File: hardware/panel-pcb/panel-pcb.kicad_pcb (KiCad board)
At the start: 4 copper layers, 127 x 127 mm, 0 parts

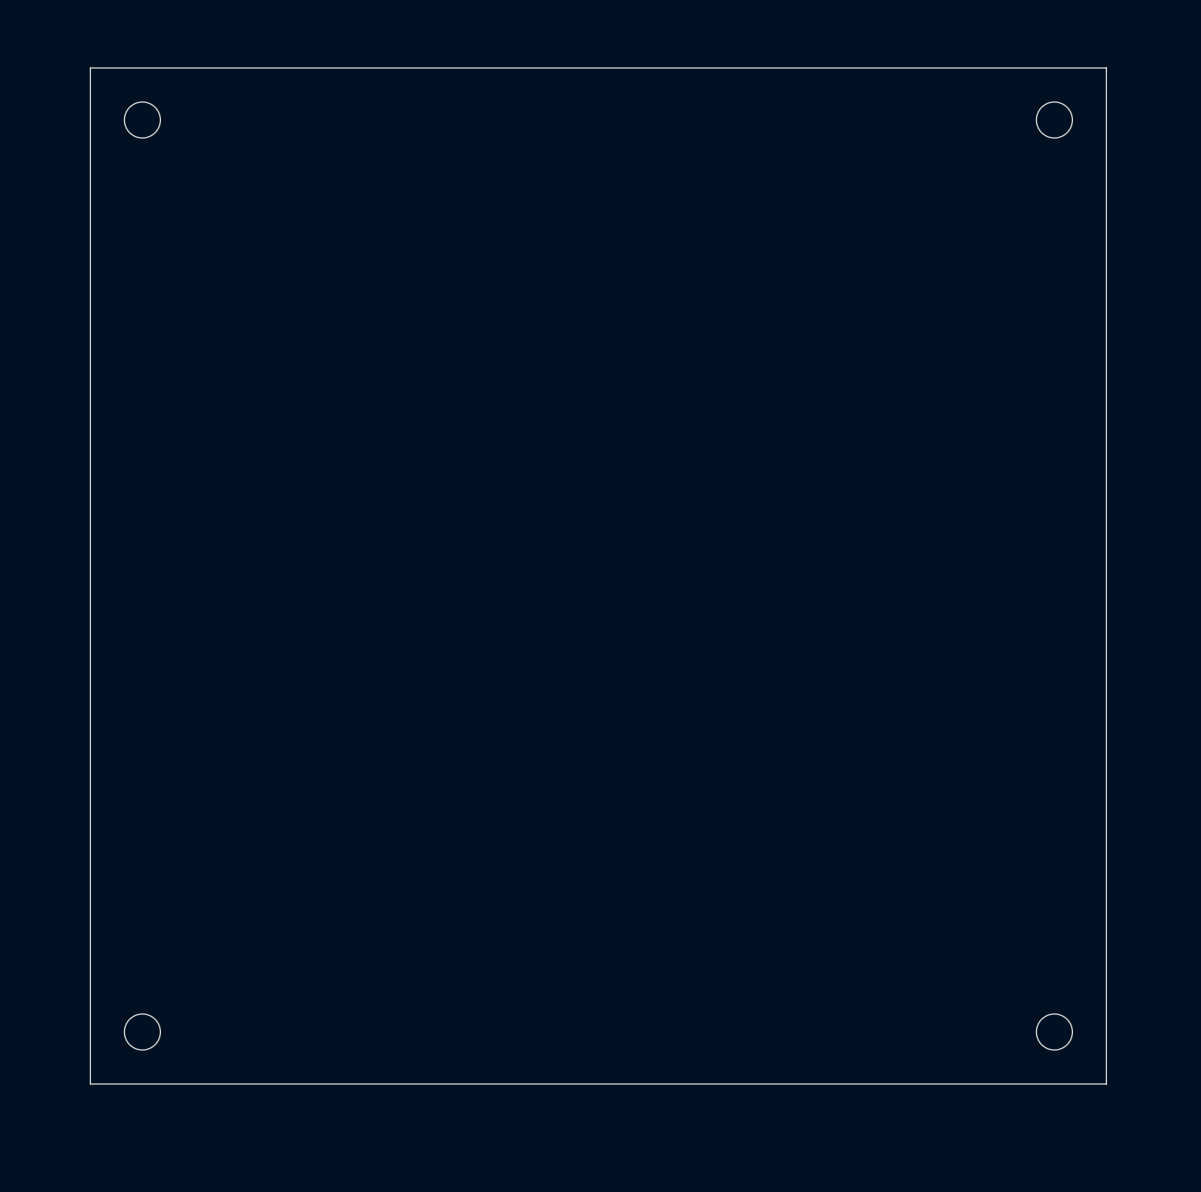
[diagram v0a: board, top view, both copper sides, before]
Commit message: PCB placement pass 1: LED lattice + all clusters
- 25x WS2815 on measured lattice (4-3-4-3-4-3-4, row 1 Y=11mm, 17mm rows,
  34mm columns, serpentine chain order derived from netlist), per-LED caps
  mid-gap below each LED
- Edge connectors at stock-measured positions (power ~25mm, INT ~93mm,
  RS-485 IN ~103mm left / OUT ~95mm right), FSR JST-PH near-centered per edge
- MCU cluster in the x148-162 lattice channel (QFN + decoupler columns,
  crystal, flash, FSR analog strip at pins), LDO cluster top-left by power IN,
  RS-485 xcvr + termination bottom-left by data connectors, shifter at LED 0,
  USB-C/SWD/BOOTSEL/ID-DIP bottom strip, TPs near their signals
- DRC: 0 shorts; remaining violations are silk/courtyard refinements
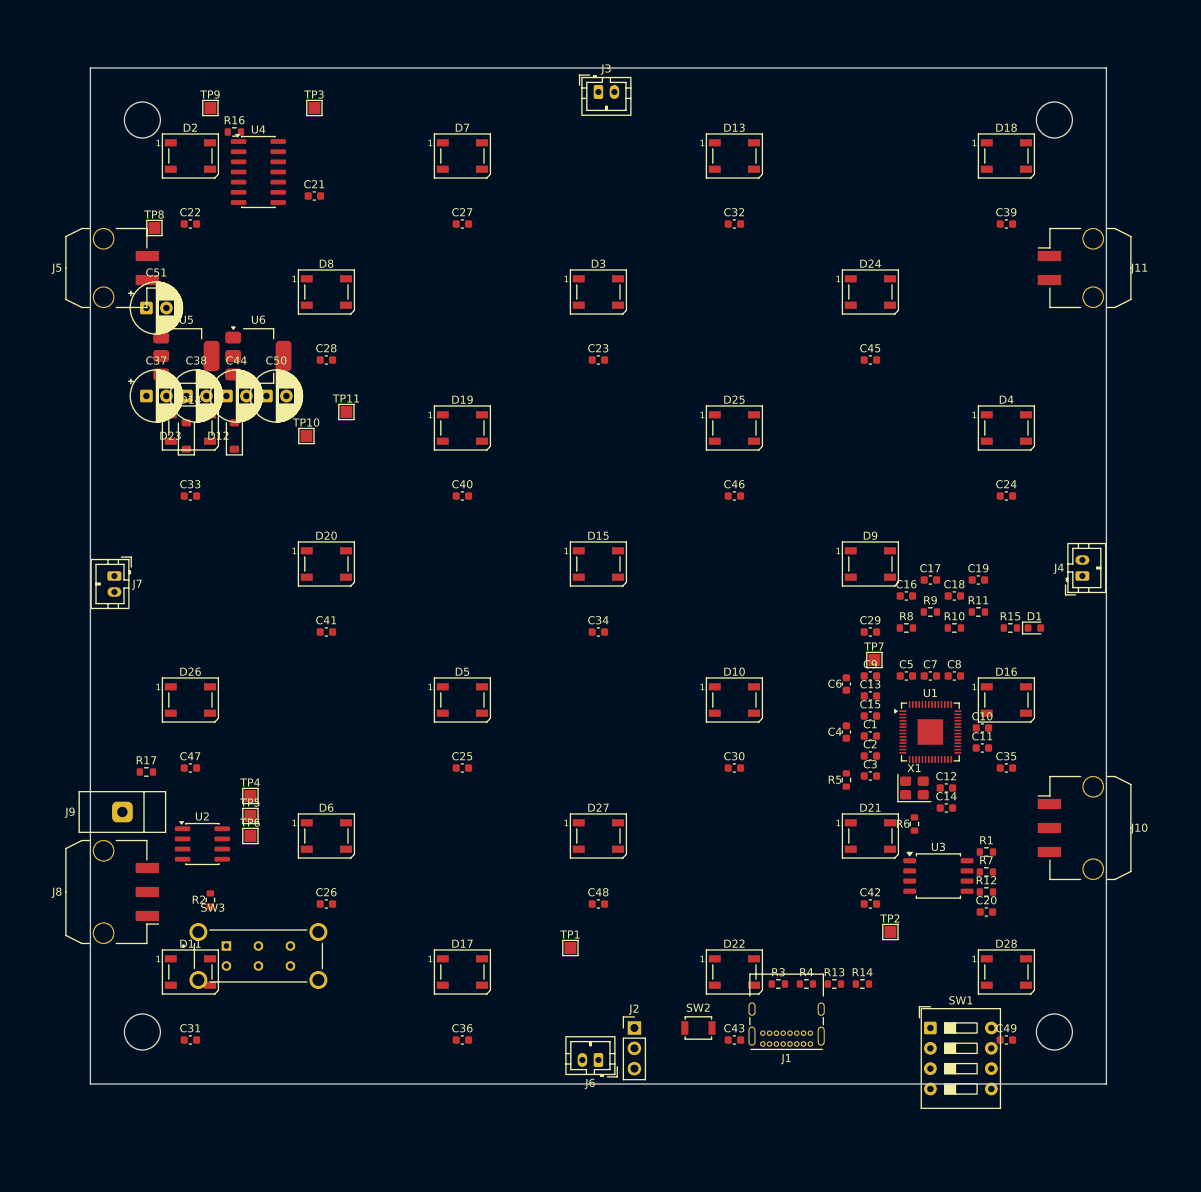
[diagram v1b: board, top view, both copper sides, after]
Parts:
- added C1: 100nF X7R 50V, Capacitor_SMD:C_0603_1608Metric, F.Cu at (147.5, 133.5)
- added C10: 100nF X7R 50V, Capacitor_SMD:C_0603_1608Metric, F.Cu at (161.5, 132.5)
- added C11: 100nF X7R 50V, Capacitor_SMD:C_0603_1608Metric, F.Cu at (161.5, 135.0)
- added C12: 15pF C0G 50V, Capacitor_SMD:C_0603_1608Metric, F.Cu at (157.0, 140.0)
- added C13: 100nF X7R 50V, Capacitor_SMD:C_0603_1608Metric, F.Cu at (147.5, 128.5)
- added C14: 15pF C0G 50V, Capacitor_SMD:C_0603_1608Metric, F.Cu at (157.0, 142.5)
- added C15: 100nF X7R 50V, Capacitor_SMD:C_0603_1608Metric, F.Cu at (147.5, 131.0)
- added C16: 10nF C0G 50V, Capacitor_SMD:C_0603_1608Metric, F.Cu at (152.0, 116.0)
- added C17: 10nF C0G 50V, Capacitor_SMD:C_0603_1608Metric, F.Cu at (155.0, 114.0)
- added C18: 10nF C0G 50V, Capacitor_SMD:C_0603_1608Metric, F.Cu at (158.0, 116.0)
- added C19: 10nF C0G 50V, Capacitor_SMD:C_0603_1608Metric, F.Cu at (161.0, 114.0)
- added C2: 100nF X7R 50V, Capacitor_SMD:C_0603_1608Metric, F.Cu at (147.5, 136.0)
- added C20: 100nF X7R 50V, Capacitor_SMD:C_0603_1608Metric, F.Cu at (162.0, 155.5)
- added C21: 100nF X7R 50V, Capacitor_SMD:C_0603_1608Metric, F.Cu at (78.0, 66.0)
- added C22: 100nF X7R 50V, Capacitor_SMD:C_0603_1608Metric, F.Cu at (62.5, 69.5)
- added C23: 100nF X7R 50V, Capacitor_SMD:C_0603_1608Metric, F.Cu at (113.5, 86.5)
- added C24: 100nF X7R 50V, Capacitor_SMD:C_0603_1608Metric, F.Cu at (164.5, 103.5)
- added C25: 100nF X7R 50V, Capacitor_SMD:C_0603_1608Metric, F.Cu at (96.5, 137.5)
- added C26: 100nF X7R 50V, Capacitor_SMD:C_0603_1608Metric, F.Cu at (79.5, 154.5)
- added C27: 100nF X7R 50V, Capacitor_SMD:C_0603_1608Metric, F.Cu at (96.5, 69.5)
- added C28: 100nF X7R 50V, Capacitor_SMD:C_0603_1608Metric, F.Cu at (79.5, 86.5)
- added C29: 100nF X7R 50V, Capacitor_SMD:C_0603_1608Metric, F.Cu at (147.5, 120.5)
- added C3: 100nF X7R 50V, Capacitor_SMD:C_0603_1608Metric, F.Cu at (147.5, 138.5)
- added C30: 100nF X7R 50V, Capacitor_SMD:C_0603_1608Metric, F.Cu at (130.5, 137.5)
- added C31: 100nF X7R 50V, Capacitor_SMD:C_0603_1608Metric, F.Cu at (62.5, 171.5)
- added C32: 100nF X7R 50V, Capacitor_SMD:C_0603_1608Metric, F.Cu at (130.5, 69.5)
- added C33: 100nF X7R 50V, Capacitor_SMD:C_0603_1608Metric, F.Cu at (62.5, 103.5)
- added C34: 100nF X7R 50V, Capacitor_SMD:C_0603_1608Metric, F.Cu at (113.5, 120.5)
- added C35: 100nF X7R 50V, Capacitor_SMD:C_0603_1608Metric, F.Cu at (164.5, 137.5)
- added C36: 100nF X7R 50V, Capacitor_SMD:C_0603_1608Metric, F.Cu at (96.5, 171.5)
- added C37: 10uF elec 25V, Capacitor_THT:CP_Radial_D6.3mm_P2.50mm, F.Cu at (57.0, 91.0)
- added C38: 22uF elec 25V, Capacitor_THT:CP_Radial_D6.3mm_P2.50mm, F.Cu at (62.0, 91.0)
- added C39: 100nF X7R 50V, Capacitor_SMD:C_0603_1608Metric, F.Cu at (164.5, 69.5)
- added C4: 2.2uF X5R 16V, Capacitor_SMD:C_0603_1608Metric, F.Cu at (144.5, 133.0)
- added C40: 100nF X7R 50V, Capacitor_SMD:C_0603_1608Metric, F.Cu at (96.5, 103.5)
- added C41: 100nF X7R 50V, Capacitor_SMD:C_0603_1608Metric, F.Cu at (79.5, 120.5)
- added C42: 100nF X7R 50V, Capacitor_SMD:C_0603_1608Metric, F.Cu at (147.5, 154.5)
- added C43: 100nF X7R 50V, Capacitor_SMD:C_0603_1608Metric, F.Cu at (130.5, 171.5)
- added C44: 10uF elec 25V, Capacitor_THT:CP_Radial_D6.3mm_P2.50mm, F.Cu at (67.0, 91.0)
- added C45: 100nF X7R 50V, Capacitor_SMD:C_0603_1608Metric, F.Cu at (147.5, 86.5)
- added C46: 100nF X7R 50V, Capacitor_SMD:C_0603_1608Metric, F.Cu at (130.5, 103.5)
- added C47: 100nF X7R 50V, Capacitor_SMD:C_0603_1608Metric, F.Cu at (62.5, 137.5)
- added C48: 100nF X7R 50V, Capacitor_SMD:C_0603_1608Metric, F.Cu at (113.5, 154.5)
- added C49: 100nF X7R 50V, Capacitor_SMD:C_0603_1608Metric, F.Cu at (164.5, 171.5)
- added C5: 100nF X7R 50V, Capacitor_SMD:C_0603_1608Metric, F.Cu at (152.0, 126.0)
- added C50: 22uF elec 25V, Capacitor_THT:CP_Radial_D6.3mm_P2.50mm, F.Cu at (72.0, 91.0)
- added C51: 470uF elec 25V, Capacitor_THT:CP_Radial_D6.3mm_P2.50mm, F.Cu at (57.0, 80.0)
- added C6: 1uF X5R 16V, Capacitor_SMD:C_0603_1608Metric, F.Cu at (144.5, 127.0)
- added C7: 100nF X7R 50V, Capacitor_SMD:C_0603_1608Metric, F.Cu at (155.0, 126.0)
- added C8: 100nF X7R 50V, Capacitor_SMD:C_0603_1608Metric, F.Cu at (158.0, 126.0)
- added C9: 1uF X5R 16V, Capacitor_SMD:C_0603_1608Metric, F.Cu at (147.5, 126.0)
- added D1: DEBUG, LED_SMD:LED_0603_1608Metric, F.Cu at (168.0, 120.0)
- added D10: WS2815, LED_SMD:LED_WS2812B_PLCC4_5.0x5.0mm_P3.2mm, F.Cu at (130.5, 129.0)
- added D11: WS2815, LED_SMD:LED_WS2812B_PLCC4_5.0x5.0mm_P3.2mm, F.Cu at (62.5, 163.0)
- added D12: 1N5819W, Diode_SMD:D_SOD-123, F.Cu at (68.0, 96.0)
- added D13: WS2815, LED_SMD:LED_WS2812B_PLCC4_5.0x5.0mm_P3.2mm, F.Cu at (130.5, 61.0)
- added D14: WS2815, LED_SMD:LED_WS2812B_PLCC4_5.0x5.0mm_P3.2mm, F.Cu at (62.5, 95.0)
- added D15: WS2815, LED_SMD:LED_WS2812B_PLCC4_5.0x5.0mm_P3.2mm, F.Cu at (113.5, 112.0)
- added D16: WS2815, LED_SMD:LED_WS2812B_PLCC4_5.0x5.0mm_P3.2mm, F.Cu at (164.5, 129.0)
- added D17: WS2815, LED_SMD:LED_WS2812B_PLCC4_5.0x5.0mm_P3.2mm, F.Cu at (96.5, 163.0)
- added D18: WS2815, LED_SMD:LED_WS2812B_PLCC4_5.0x5.0mm_P3.2mm, F.Cu at (164.5, 61.0)
- added D19: WS2815, LED_SMD:LED_WS2812B_PLCC4_5.0x5.0mm_P3.2mm, F.Cu at (96.5, 95.0)
- added D2: WS2815, LED_SMD:LED_WS2812B_PLCC4_5.0x5.0mm_P3.2mm, F.Cu at (62.5, 61.0)
- added D20: WS2815, LED_SMD:LED_WS2812B_PLCC4_5.0x5.0mm_P3.2mm, F.Cu at (79.5, 112.0)
- added D21: WS2815, LED_SMD:LED_WS2812B_PLCC4_5.0x5.0mm_P3.2mm, F.Cu at (147.5, 146.0)
- added D22: WS2815, LED_SMD:LED_WS2812B_PLCC4_5.0x5.0mm_P3.2mm, F.Cu at (130.5, 163.0)
- added D23: 1N5819W, Diode_SMD:D_SOD-123, F.Cu at (62.0, 96.0)
- added D24: WS2815, LED_SMD:LED_WS2812B_PLCC4_5.0x5.0mm_P3.2mm, F.Cu at (147.5, 78.0)
- added D25: WS2815, LED_SMD:LED_WS2812B_PLCC4_5.0x5.0mm_P3.2mm, F.Cu at (130.5, 95.0)
- added D26: WS2815, LED_SMD:LED_WS2812B_PLCC4_5.0x5.0mm_P3.2mm, F.Cu at (62.5, 129.0)
- added D27: WS2815, LED_SMD:LED_WS2812B_PLCC4_5.0x5.0mm_P3.2mm, F.Cu at (113.5, 146.0)
- added D28: WS2815, LED_SMD:LED_WS2812B_PLCC4_5.0x5.0mm_P3.2mm, F.Cu at (164.5, 163.0)
- added D3: WS2815, LED_SMD:LED_WS2812B_PLCC4_5.0x5.0mm_P3.2mm, F.Cu at (113.5, 78.0)
- added D4: WS2815, LED_SMD:LED_WS2812B_PLCC4_5.0x5.0mm_P3.2mm, F.Cu at (164.5, 95.0)
- added D5: WS2815, LED_SMD:LED_WS2812B_PLCC4_5.0x5.0mm_P3.2mm, F.Cu at (96.5, 129.0)
- added D6: WS2815, LED_SMD:LED_WS2812B_PLCC4_5.0x5.0mm_P3.2mm, F.Cu at (79.5, 146.0)
- added D7: WS2815, LED_SMD:LED_WS2812B_PLCC4_5.0x5.0mm_P3.2mm, F.Cu at (96.5, 61.0)
- added D8: WS2815, LED_SMD:LED_WS2812B_PLCC4_5.0x5.0mm_P3.2mm, F.Cu at (79.5, 78.0)
- added D9: WS2815, LED_SMD:LED_WS2812B_PLCC4_5.0x5.0mm_P3.2mm, F.Cu at (147.5, 112.0)
- added J1: USB_C_Receptacle_USB2.0_16P, Connector_USB:USB_C_Receptacle_GCT_USB4085, F.Cu at (140.0, 172.0)
- added J10: RS-485 OUT, Connector_Molex:Molex_Micro-Fit_3.0_43650-0310_1x03-1MP_P3.00mm_Horizontal, F.Cu at (175.0, 145.0)
- added J11: 12V_OUT, Connector_Molex:Molex_Micro-Fit_3.0_43650-0210_1x02-1MP_P3.00mm_Horizontal, F.Cu at (175.0, 75.0)
- added J2: SWD, Connector_PinHeader_2.54mm:PinHeader_1x03_P2.54mm_Vertical, F.Cu at (118.0, 170.0)
- added J3: FSR North, Connector_JST:JST_PH_B2B-PH-K_1x02_P2.00mm_Vertical, F.Cu at (113.5, 53.0)
- added J4: FSR East, Connector_JST:JST_PH_B2B-PH-K_1x02_P2.00mm_Vertical, F.Cu at (174.0, 113.5)
- added J5: 12V_IN, Connector_Molex:Molex_Micro-Fit_3.0_43650-0210_1x02-1MP_P3.00mm_Horizontal, F.Cu at (52.0, 75.0)
- added J6: FSR South, Connector_JST:JST_PH_B2B-PH-K_1x02_P2.00mm_Vertical, F.Cu at (113.5, 174.0)
- added J7: FSR West, Connector_JST:JST_PH_B2B-PH-K_1x02_P2.00mm_Vertical, F.Cu at (53.0, 113.5)
- added J8: RS-485 IN, Connector_Molex:Molex_Micro-Fit_3.0_43650-0310_1x03-1MP_P3.00mm_Horizontal, F.Cu at (52.0, 153.0)
- added J9: INT OUT, panel-pcb:TerminalBlock_KF301-1P_P5.08mm, F.Cu at (54.0, 143.0)
- added R1: 10k, Resistor_SMD:R_0603_1608Metric, F.Cu at (162.0, 148.0)
- added R10: 10k 1%, Resistor_SMD:R_0603_1608Metric, F.Cu at (158.0, 120.0)
- added R11: 10k 1%, Resistor_SMD:R_0603_1608Metric, F.Cu at (161.0, 118.0)
- added R12: 10k DNF, Resistor_SMD:R_0603_1608Metric, F.Cu at (162.0, 153.0)
- added R13: 5.1k, Resistor_SMD:R_0603_1608Metric, F.Cu at (143.0, 164.5)
- added R14: 5.1k, Resistor_SMD:R_0603_1608Metric, F.Cu at (146.5, 164.5)
- added R15: 1k, Resistor_SMD:R_0603_1608Metric, F.Cu at (165.0, 120.0)
- added R16: 330R, Resistor_SMD:R_0603_1608Metric, F.Cu at (68.0, 58.0)
- added R17: 100R, Resistor_SMD:R_0603_1608Metric, F.Cu at (57.0, 138.0)
- added R2: 120R, Resistor_SMD:R_0603_1608Metric, F.Cu at (65.0, 154.0)
- added R3: 27R 1%, Resistor_SMD:R_0603_1608Metric, F.Cu at (136.0, 164.5)
- added R4: 27R 1%, Resistor_SMD:R_0603_1608Metric, F.Cu at (139.5, 164.5)
- added R5: 201R 1%, Resistor_SMD:R_0603_1608Metric, F.Cu at (144.5, 139.0)
- added R6: 1k 1%, Resistor_SMD:R_0603_1608Metric, F.Cu at (153.0, 144.5)
- added R7: 1k, Resistor_SMD:R_0603_1608Metric, F.Cu at (162.0, 150.5)
- added R8: 10k 1%, Resistor_SMD:R_0603_1608Metric, F.Cu at (152.0, 120.0)
- added R9: 10k 1%, Resistor_SMD:R_0603_1608Metric, F.Cu at (155.0, 118.0)
- added SW1: PANEL_ID, Button_Switch_THT:SW_DIP_SPSTx04_Slide_9.78x12.34mm_W7.62mm_P2.54mm, F.Cu at (155.0, 170.0)
- added SW2: BOOTSEL, Button_Switch_SMD:SW_SPST_B3U-1000P, F.Cu at (126.0, 170.0)
- added SW3: RS-485 Termination, panel-pcb:SW_EG2201A, F.Cu at (71.0, 161.0)
- added TP1: RUN, TestPoint:TestPoint_Pad_1.5x1.5mm, F.Cu at (110.0, 160.0)
- added TP10: +5.0V, TestPoint:TestPoint_Pad_1.5x1.5mm, F.Cu at (77.0, 96.0)
- added TP11: +3V3, TestPoint:TestPoint_Pad_1.5x1.5mm, F.Cu at (82.0, 93.0)
- added TP2: GND, TestPoint:TestPoint_Pad_1.5x1.5mm, F.Cu at (150.0, 158.0)
- added TP3: GND, TestPoint:TestPoint_Pad_1.5x1.5mm, F.Cu at (78.0, 55.0)
- added TP4: UART RX, TestPoint:TestPoint_Pad_1.5x1.5mm, F.Cu at (70.0, 141.0)
- added TP5: UART TX, TestPoint:TestPoint_Pad_1.5x1.5mm, F.Cu at (70.0, 143.5)
- added TP6: RS-485 DC, TestPoint:TestPoint_Pad_1.5x1.5mm, F.Cu at (70.0, 146.0)
- added TP7: LED Data 3.3V, TestPoint:TestPoint_Pad_1.5x1.5mm, F.Cu at (148.0, 124.0)
- added TP8: +12.0V, TestPoint:TestPoint_Pad_1.5x1.5mm, F.Cu at (58.0, 70.0)
- added TP9: LED Data 5.0V, TestPoint:TestPoint_Pad_1.5x1.5mm, F.Cu at (65.0, 55.0)
- added U1: RP2040, Package_DFN_QFN:QFN-56-1EP_7x7mm_P0.4mm_EP3.2x3.2mm, F.Cu at (155.0, 133.0)
- added U2: THVD1419, Package_SO:SOIC-8_3.9x4.9mm_P1.27mm, F.Cu at (64.0, 147.0)
- added U3: W25Q32JV, Package_SO:SOIC-8_5.3x5.3mm_P1.27mm, F.Cu at (156.0, 151.0)
- added U4: SN74AHCT125, Package_SO:SOIC-14_3.9x8.7mm_P1.27mm, F.Cu at (71.0, 63.0)
- added U5: AMS1117-5.0, Package_TO_SOT_SMD:SOT-223-3_TabPin2, F.Cu at (62.0, 86.0)
- added U6: AMS1117-3.3, Package_TO_SOT_SMD:SOT-223-3_TabPin2, F.Cu at (71.0, 86.0)
- added X1: 12MHz, Crystal:Crystal_SMD_3225-4Pin_3.2x2.5mm, F.Cu at (153.0, 140.0)

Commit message: Board outline: stock-style connector tabs + user placement pass
- 5 tabs, 4mm deep, sized to final connector positions: left power (y67-83),
  merged left INT+RS-485 (y132-162, like stock's stepped lower-left), right
  power (y67-83), right RS-485 (y143-163), bottom USB (x145.5-159.5)
- J5/J8/J9/J10/J11/J1 shifted 4mm outward onto their tabs
- Includes user's GUI placement adjustments (KiCad 10 format)
- DRC: 0 shorts, 96 violations (was 512) - remaining are silk refinements +
  by-design no-net peg pads near tab faces
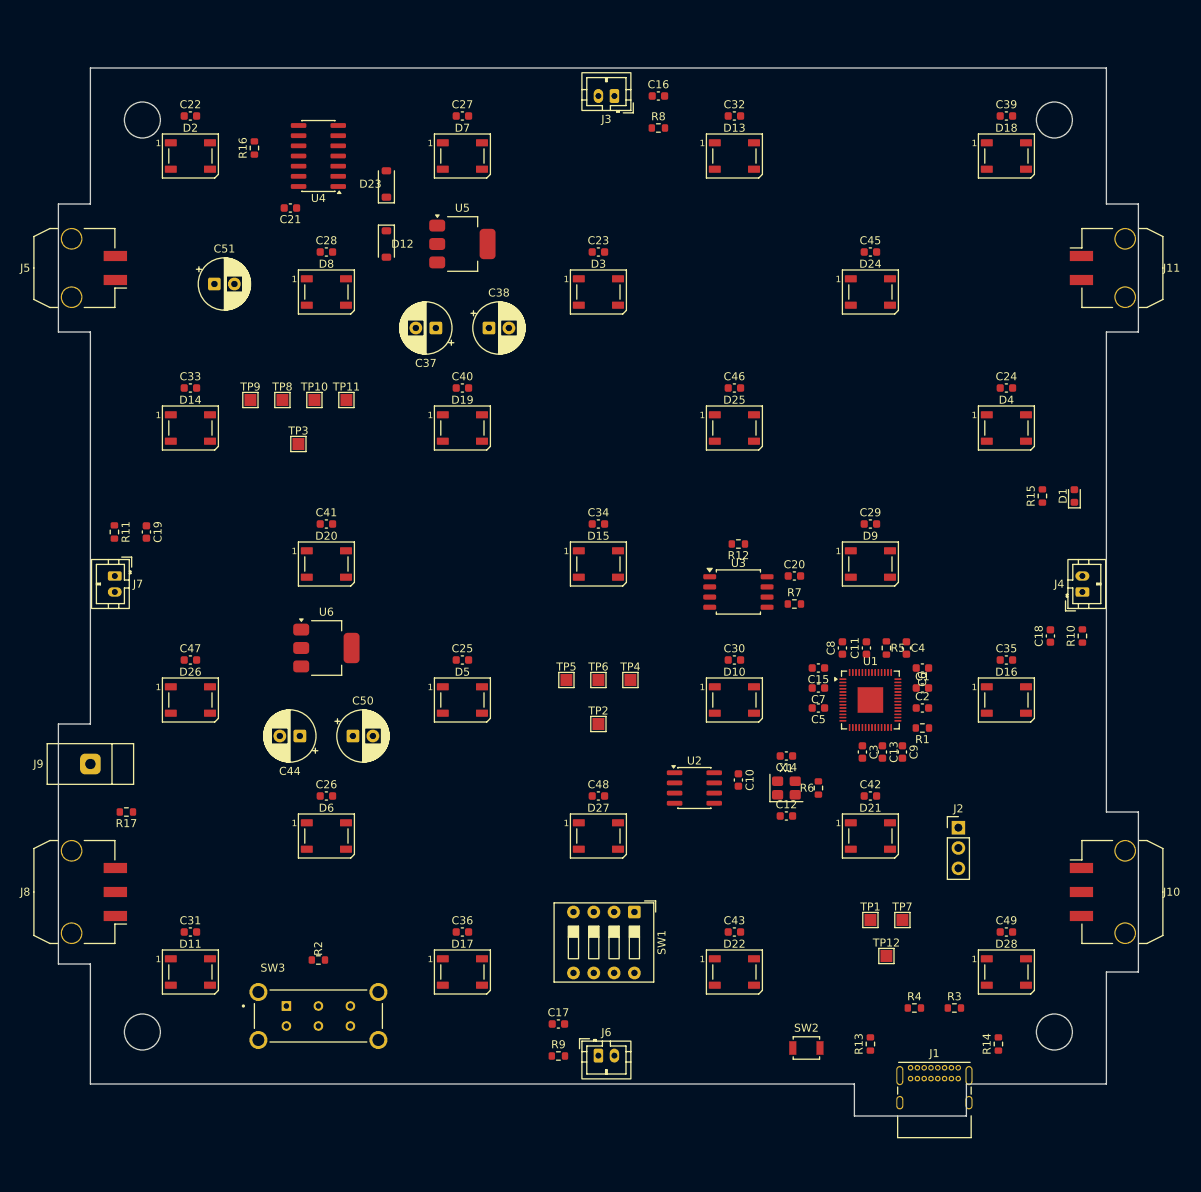
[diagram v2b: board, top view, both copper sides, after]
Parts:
- added TP12: GND, TestPoint:TestPoint_Pad_1.5x1.5mm, F.Cu at (149.5, 161.0)
- moved R11 108.5 mm to (53.0, 108.0), turned to -90 degrees
- moved C19 104.2 mm to (57.0, 108.0), turned to -90 degrees
- moved C17 72.4 mm to (108.5, 169.5)
- moved R9 72.4 mm to (108.5, 173.5)
- moved C16 69.8 mm to (121.0, 53.5)
- moved R8 69.8 mm to (121.0, 57.5)
- moved U2 61.9 mm to (125.5, 140.0)
- moved R12 53.4 mm to (131.0, 109.5), turned to 180 degrees
- moved TP4 49.7 mm to (117.5, 126.5)
- moved C20 48.4 mm to (138.0, 113.5)
- moved TP6 47.7 mm to (113.5, 126.5)
- moved J2 47.6 mm to (158.5, 145.0)
- moved TP2 44.8 mm to (113.5, 132.0)
- moved C50 43.9 mm to (82.8, 133.5)
- moved C44 43.5 mm to (76.2, 133.5), turned to 180 degrees
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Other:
- board size 127 x 127 mm -> 135 x 131 mm

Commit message: Panel PCB: refined mounting hole/LED lattice measurements, 0402 RP2040 decoupling, JLC DRC rules
- Mounting holes: top pair 113mm apart (not a symmetric 114mm square) per
  refined caliper measurement, cross-checked against the stock board photo.
- LED lattice: 33.5mm column pitch (not 34mm), 17mm row pitch, insets
  13.5/13.0mm (L/R) and 12.5mm (T/B) - only the 25 LED footprints moved.
- RP2040 decoupling caps (C1,C2,C3,C4,C5,C6,C7,C8,C9,C11,C13,C15): 0603 -> 0402
  for placement clearance; nets/positions preserved.
- Added JLCPCB 4-layer custom DRC rules (panel-pcb.kicad_dru) and matching
  Board Setup constraint values.
- Added corrected WS2815 PLCC6 footprint (panel-pcb.pretty/) with pad
  numbering matched to the real WS2815 datasheet pinout - the previously
  assigned LED_WS2812B_PLCC4 footprint only had 4 pads for a 6-pin part
  (GND and BIN were unrealized), and KiCad's stock LED_WS2812_PLCC6
  footprint is for a different chip with incompatible pin numbering.
  Not yet applied to the 25 LED instances.
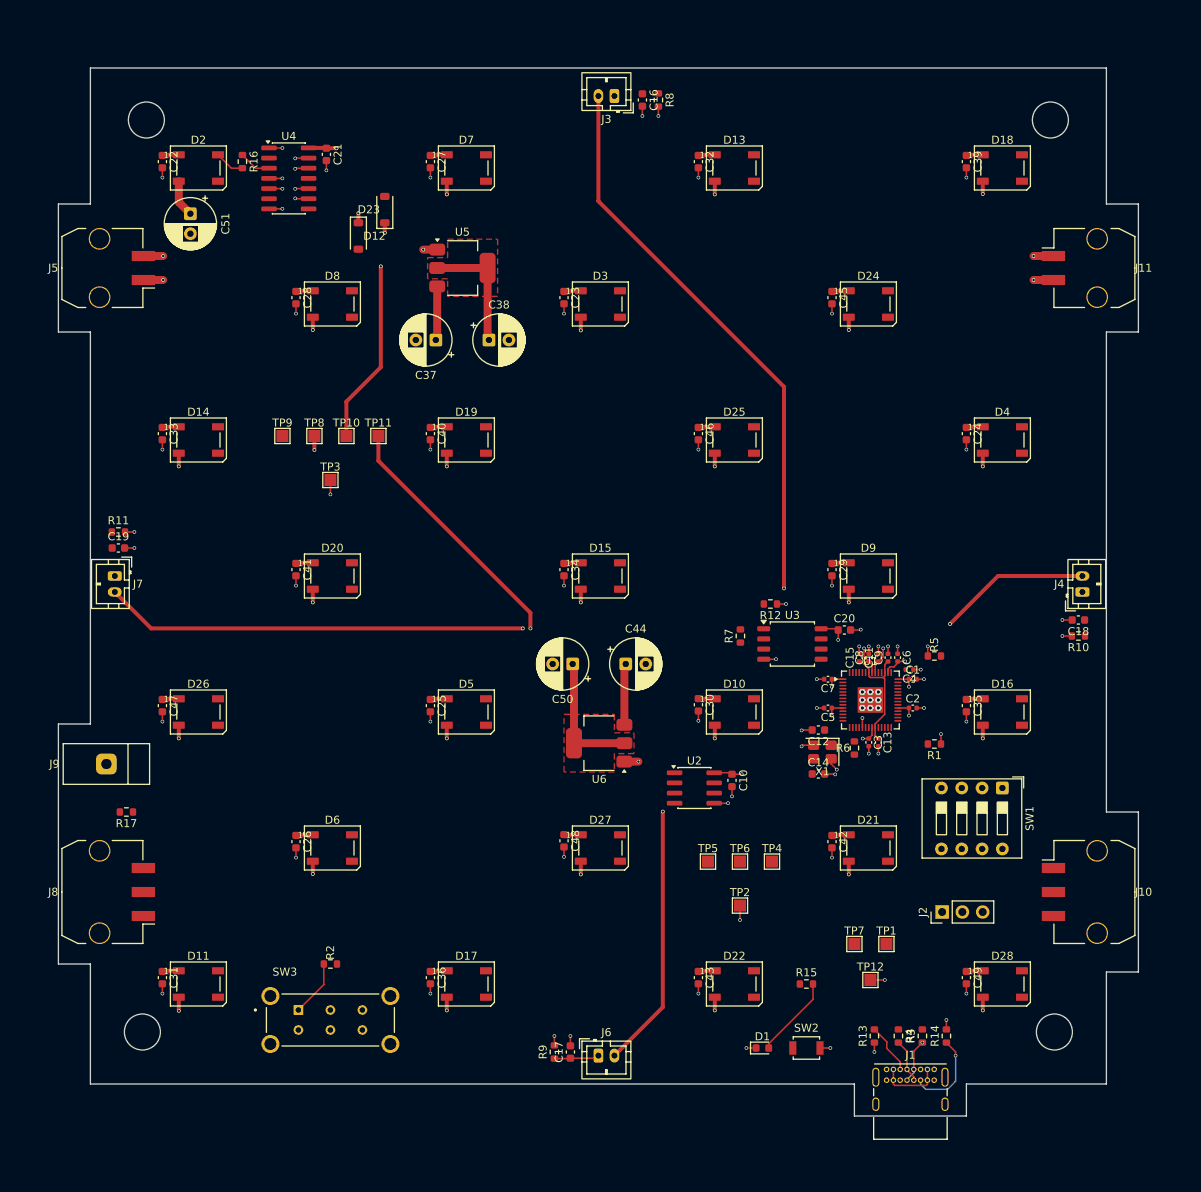
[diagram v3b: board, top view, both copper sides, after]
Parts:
- C1, C11, C13, C15, C2, C3, C4, C5, C6, C7, C8, C9: footprint Capacitor_SMD:C_0603_1608Metric -> Capacitor_SMD:C_0402_1005Metric
- moved D1 79.3 mm to (134.0, 172.5), turned to 0 degrees
- moved R15 67.8 mm to (139.5, 164.5), turned to 0 degrees
- moved SW1 48.5 mm to (164.0, 140.0)
- moved C44 41.7 mm to (116.9, 124.5), turned to 0 degrees
- moved U6 36.1 mm to (113.6, 134.4), turned to 180 degrees
- moved C50 28.9 mm to (110.3, 124.5), turned to 180 degrees
- moved TP5 28.8 mm to (127.2, 149.2)
- moved TP2 28.8 mm to (131.2, 154.7)
- moved TP4 28.8 mm to (135.2, 149.2)
- moved TP6 28.8 mm to (131.2, 149.2)
- moved C9 11.9 mm to (149.7, 123.7), turned to 90 degrees
- moved C12 11.5 mm to (141.0, 132.8), turned to 180 degrees
- moved J2 10.7 mm to (156.5, 155.5), turned to 90 degrees
- moved U3 9.37 mm to (137.8, 122.0)
- moved C51 9.28 mm to (62.5, 68.2), turned to -90 degrees
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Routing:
- net +3V3: track 0.00 -> 256.4 mm, vias 0 -> 18
- net GND: track 0.00 -> 97.6 mm, vias 0 -> 83
- net +12.0V: track 0.00 -> 57.6 mm, vias 0 -> 27
- net +5.0V: track 0.00 -> 36.6 mm, vias 0 -> 4
- net Net-(D23-A): track 0.00 -> 15.4 mm
- net +1.1V: track 0.00 -> 15.0 mm
- net Net-(J1-CC2): track 0.00 -> 10.8 mm, vias 0 -> 1
- net Net-(D1-A): track 0.00 -> 10.3 mm
- net VBUS: track 0.00 -> 8.08 mm, vias 0 -> 1
- net Net-(R2-Pad1): track 0.00 -> 7.07 mm
- net Net-(J1-CC1): track 0.00 -> 6.34 mm
- net GPIO28/ADC2: track 0.00 -> 5.66 mm
- net USB_DP: track 0.00 -> 5.50 mm
- net USB_DM: track 0.00 -> 5.50 mm, vias 0 -> 1
- net Net-(R16-Pad1): track 0.00 -> 4.01 mm
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- added copper zone on In2.Cu, net +12.0V
- added copper zone on F.Cu, net +3V3
- added copper zone on In2.Cu, net +3V3
- added copper zone on In2.Cu, net +5.0V
- added copper zone on In1.Cu, net GND
- added copper zone on F.Cu, net Net-(D23-A)
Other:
- outline, holes or cut-outs redrawn
